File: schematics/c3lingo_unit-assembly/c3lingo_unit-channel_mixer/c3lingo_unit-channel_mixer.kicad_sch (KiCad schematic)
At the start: 94 parts, among them J301 Interconnect, J302 PowerSupply, J303 I/O, Q301 MMBFJ113, SW301 OnAir_X, SW302 Mute_X, U301 TL072, U302 LM339, U303 LM339, U304 LM339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

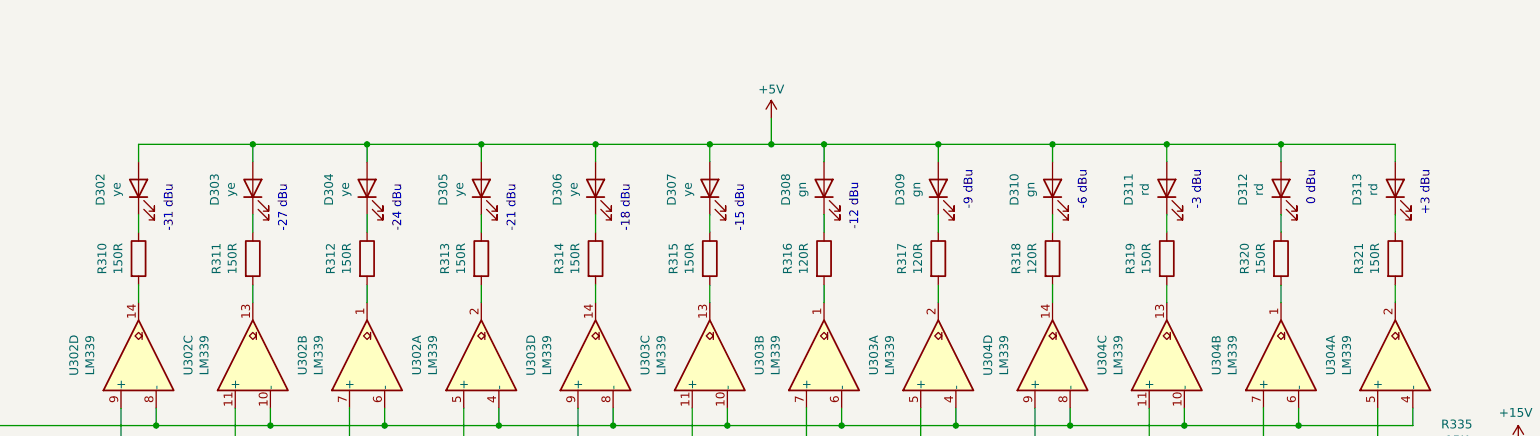
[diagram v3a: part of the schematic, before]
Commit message: Channel-Mixer: Change VU meter LEDs footprint to 5x2mm THD
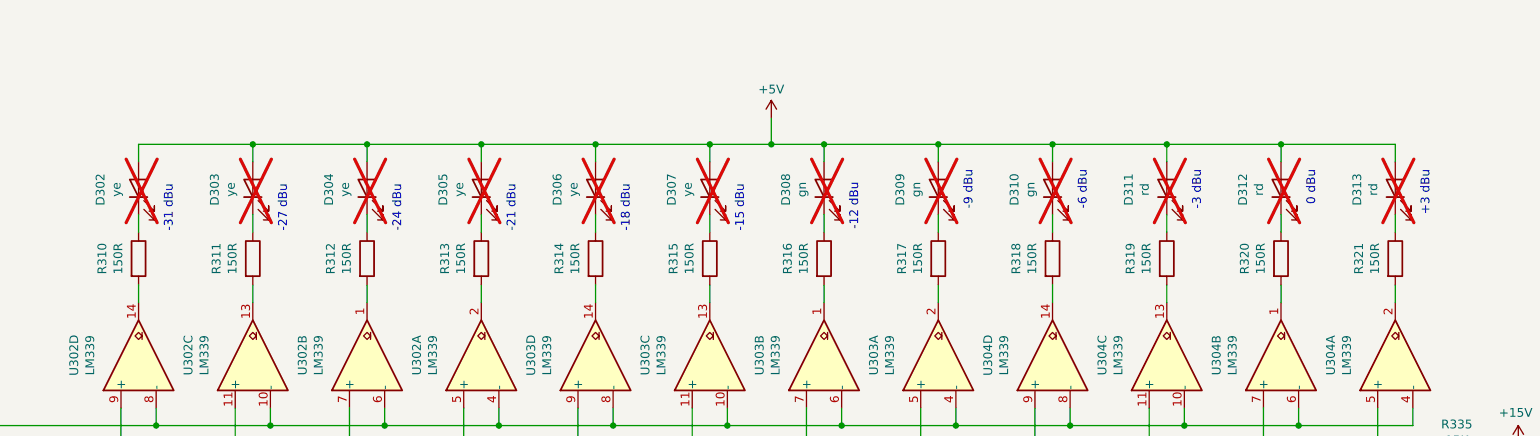
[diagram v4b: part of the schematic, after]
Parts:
- D302, D303, D304, D305, D306, D307: footprint LED_SMD:LED_0805_2012Metric_Pad1.15x1.40mm_HandSolder -> LED_THT:LED_Rectangular_W5.0mm_H2.0mm; LCSC Part # C2296 -> (none); Model generic 20 mA, 2.1 V -> LTL-433Y (2.1 V, 20 mA) or WP113YDT (2.0 V, 20 mA); now not fitted
- D308, D309, D310: footprint LED_SMD:LED_0805_2012Metric_Pad1.15x1.40mm_HandSolder -> LED_THT:LED_Rectangular_W5.0mm_H2.0mm; Model generic 20 mA, 2.8-2.9 V -> LTL433G or WP113GDT (2.2 V, 20 mA); now not fitted
- D311, D312, D313: footprint LED_SMD:LED_0805_2012Metric_Pad1.15x1.40mm_HandSolder -> LED_THT:LED_Rectangular_W5.0mm_H2.0mm; LCSC Part # C84256 -> (none); Model generic 20 mA, 2.0 V -> LTL433HR or WP113IDT (2.0 V, 20 mA); now not fitted
- R316, R317, R318: value 120R -> 150R
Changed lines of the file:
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@@
 	(title_block
 		(title "c3lingo interpeter unit -- channel mixer")
-		(date "2024-12-18")
+		(date "2025-08-25")
 		(rev "v0.4.0-dev")
 		(company "Jannik Beyerstedt (jtbx)")
@@
 		(in_bom yes)
 		(on_board yes)
-		(dnp no)
+		(dnp yes)
 		(property "Reference" "D313"
 			(at 332.3082 156.3878 0)
@@
 			)
 		)
-		(property "Footprint" "LED_SMD:LED_0805_2012Metric_Pad1.15x1.40mm_HandSolder"
+		(property "Footprint" "LED_THT:LED_Rectangular_W5.0mm_H2.0mm"
 			(at 337.82 156.21 0)
 			(effects
@@
 			)
 		)
-		(property "Model" "generic 20 mA, 2.0 V"
+		(property "Model" "LTL433HR or WP113IDT (2.0 V, 20 mA)"
 			(at 337.82 156.21 0)
 			(effects
@@
 			)
 		)
-		(property "LCSC Part #" "C84256"
+		(property "LCSC Part #" ""
 			(at 337.82 156.21 0)
 			(effects
@@
 		(in_bom yes)
 		(on_board yes)
-		(dnp no)
+		(dnp yes)
 		(property "Reference" "D312"
 			(at 315.7982 156.3878 0)
@@
 			)
 		)
-		(property "Footprint" "LED_SMD:LED_0805_2012Metric_Pad1.15x1.40mm_HandSolder"
+		(property "Footprint" "LED_THT:LED_Rectangular_W5.0mm_H2.0mm"
 			(at 321.31 156.21 0)
 			(effects
@@
 			)
 		)
-		(property "Model" "generic 20 mA, 2.0 V"
+		(property "Model" "LTL433HR or WP113IDT (2.0 V, 20 mA)"
 			(at 321.31 156.21 0)
 			(effects
@@
 			)
 		)
-		(property "LCSC Part #" "C84256"
+		(property "LCSC Part #" ""
 			(at 321.31 156.21 0)
 			(effects
@@
 		(in_bom yes)
 		(on_board yes)
-		(dnp no)
+		(dnp yes)
 		(property "Reference" "D311"
 			(at 299.2882 156.3878 0)
@@
 			)
 		)
-		(property "Footprint" "LED_SMD:LED_0805_2012Metric_Pad1.15x1.40mm_HandSolder"
+		(property "Footprint" "LED_THT:LED_Rectangular_W5.0mm_H2.0mm"
 			(at 304.8 156.21 0)
 			(effects
@@
 			)
 		)
-		(property "Model" "generic 20 mA, 2.0 V"
+		(property "Model" "LTL433HR or WP113IDT (2.0 V, 20 mA)"
 			(at 304.8 156.21 0)
 			(effects
@@
 			)
 		)
-		(property "LCSC Part #" "C84256"
+		(property "LCSC Part #" ""
 			(at 304.8 156.21 0)
 			(effects
@@
 			)
 		)
-		(property "Value" "120R"
+		(property "Value" "150R"
 			(at 285.3436 166.37 90)
 			(effects
@@
 		(in_bom yes)
 		(on_board yes)
-		(dnp no)
+		(dnp yes)
 		(property "Reference" "D310"
 			(at 282.7782 156.3878 0)
@@
 			)
 		)
-		(property "Footprint" "LED_SMD:LED_0805_2012Metric_Pad1.15x1.40mm_HandSolder"
+		(property "Footprint" "LED_THT:LED_Rectangular_W5.0mm_H2.0mm"
 			(at 288.29 156.21 0)
 			(effects
@@
 			)
 		)
-		(property "Description" "needs 110R @5V"
+		(property "Description" "needs 150R @5V"
 			(at 288.29 156.21 0)
 			(effects
@@
 			)
 		)
-		(property "Model" "generic 20 mA, 2.8-2.9 V"
+		(property "Model" "LTL433G or WP113GDT (2.2 V, 20 mA)"
 			(at 288.29 156.21 0)
 			(effects
@@
 			)
 		)
-		(property "Value" "120R"
+		(property "Value" "150R"
 			(at 268.8336 166.37 90)
 			(effects
@@
 		(in_bom yes)
 		(on_board yes)
-		(dnp no)
+		(dnp yes)
 		(property "Reference" "D309"
 			(at 266.2682 156.3878 0)
@@
 			)
 		)
-		(property "Footprint" "LED_SMD:LED_0805_2012Metric_Pad1.15x1.40mm_HandSolder"
+		(property "Footprint" "LED_THT:LED_Rectangular_W5.0mm_H2.0mm"
 			(at 271.78 156.21 0)
 			(effects
@@
 			)
 		)
-		(property "Description" "needs 110R @5V"
+		(property "Description" "needs 150R @5V"
 			(at 271.78 156.21 0)
 			(effects
@@
 			)
 		)
-		(property "Model" "generic 20 mA, 2.8-2.9 V"
+		(property "Model" "LTL433G or WP113GDT (2.2 V, 20 mA)"
 			(at 271.78 156.21 0)
 			(effects
@@
 			)
 		)
-		(property "Value" "120R"
+		(property "Value" "150R"
 			(at 252.3236 166.37 90)
 			(effects
@@
 		(in_bom yes)
 		(on_board yes)
-		(dnp no)
+		(dnp yes)
 		(property "Reference" "D308"
 			(at 249.7582 156.3878 0)
@@
 			)
 		)
-		(property "Footprint" "LED_SMD:LED_0805_2012Metric_Pad1.15x1.40mm_HandSolder"
+		(property "Footprint" "LED_THT:LED_Rectangular_W5.0mm_H2.0mm"
 			(at 255.27 156.21 0)
 			(effects
@@
 			)
 		)
-		(property "Description" "needs 110R @5V"
+		(property "Description" "needs 150R @5V"
 			(at 255.27 156.21 0)
 			(effects
@@
 			)
 		)
-		(property "Model" "generic 20 mA, 2.8-2.9 V"
+		(property "Model" "LTL433G or WP113GDT (2.2 V, 20 mA)"
 			(at 255.27 156.21 0)
 			(effects
@@
 		(in_bom yes)
 		(on_board yes)
-		(dnp no)
+		(dnp yes)
 		(property "Reference" "D307"
 			(at 233.2482 156.3878 0)
@@
 			)
 		)
-		(property "Footprint" "LED_SMD:LED_0805_2012Metric_Pad1.15x1.40mm_HandSolder"
+		(property "Footprint" "LED_THT:LED_Rectangular_W5.0mm_H2.0mm"
 			(at 238.76 156.21 0)
 			(effects
@@
 			)
 		)
-		(property "Description" "needs 145R @5V"
+		(property "Description" "needs 150R @5V"
 			(at 238.76 156.21 0)
 			(effects
@@
 			)
 		)
-		(property "Model" "generic 20 mA, 2.1 V"
+		(property "Model" "LTL-433Y (2.1 V, 20 mA) or WP113YDT (2.0 V, 20 mA)"
 			(at 238.76 156.21 0)
 			(effects
@@
 			)
 		)
-		(property "LCSC Part #" "C2296"
+		(property "LCSC Part #" ""
 			(at 238.76 156.21 0)
 			(effects
@@
 		(in_bom yes)
 		(on_board yes)
-		(dnp no)
+		(dnp yes)
 		(property "Reference" "D306"
 			(at 216.7382 156.3878 0)
@@
 			)
 		)
-		(property "Footprint" "LED_SMD:LED_0805_2012Metric_Pad1.15x1.40mm_HandSolder"
+		(property "Footprint" "LED_THT:LED_Rectangular_W5.0mm_H2.0mm"
 			(at 222.25 156.21 0)
 			(effects
@@
 			)
 		)
-		(property "Description" "needs 145R @5V"
+		(property "Description" "needs 150R @5V"
 			(at 222.25 156.21 0)
 			(effects
@@
 			)
 		)
-		(property "Model" "generic 20 mA, 2.1 V"
+		(property "Model" "LTL-433Y (2.1 V, 20 mA) or WP113YDT (2.0 V, 20 mA)"
 			(at 222.25 156.21 0)
 			(effects
@@
 			)
 		)
-		(property "LCSC Part #" "C2296"
+		(property "LCSC Part #" ""
 			(at 222.25 156.21 0)
 			(effects
@@
 		(in_bom yes)
 		(on_board yes)
-		(dnp no)
+		(dnp yes)
 		(property "Reference" "D305"
 			(at 200.2282 156.3878 0)
@@
 			)
 		)
-		(property "Footprint" "LED_SMD:LED_0805_2012Metric_Pad1.15x1.40mm_HandSolder"
+		(property "Footprint" "LED_THT:LED_Rectangular_W5.0mm_H2.0mm"
 			(at 205.74 156.21 0)
 			(effects
@@
 			)
 		)
-		(property "Description" "needs 145R @5V"
+		(property "Description" "needs 150R @5V"
 			(at 205.74 156.21 0)
 			(effects
@@
 			)
 		)
-		(property "Model" "generic 20 mA, 2.1 V"
+		(property "Model" "LTL-433Y (2.1 V, 20 mA) or WP113YDT (2.0 V, 20 mA)"
 			(at 205.74 156.21 0)
 			(effects
@@
 			)
 		)
-		(property "LCSC Part #" "C2296"
+		(property "LCSC Part #" ""
 			(at 205.74 156.21 0)
 			(effects
@@
 		(in_bom yes)
 		(on_board yes)
-		(dnp no)
+		(dnp yes)
 		(property "Reference" "D304"
 			(at 183.7182 156.3878 0)
@@
 			)
 		)
-		(property "Footprint" "LED_SMD:LED_0805_2012Metric_Pad1.15x1.40mm_HandSolder"
+		(property "Footprint" "LED_THT:LED_Rectangular_W5.0mm_H2.0mm"
 			(at 189.23 156.21 0)
 			(effects
@@
 			)
 		)
-		(property "Description" "needs 145R @5V"
+		(property "Description" "needs 150R @5V"
 			(at 189.23 156.21 0)
 			(effects
@@
 			)
 		)
-		(property "Model" "generic 20 mA, 2.1 V"
+		(property "Model" "LTL-433Y (2.1 V, 20 mA) or WP113YDT (2.0 V, 20 mA)"
 			(at 189.23 156.21 0)
 			(effects
@@
 			)
 		)
-		(property "LCSC Part #" "C2296"
+		(property "LCSC Part #" ""
 			(at 189.23 156.21 0)
 			(effects
@@
 		(in_bom yes)
 		(on_board yes)
-		(dnp no)
+		(dnp yes)
 		(property "Reference" "D303"
 			(at 167.2082 156.3878 0)
@@
 			)
 		)
-		(property "Footprint" "LED_SMD:LED_0805_2012Metric_Pad1.15x1.40mm_HandSolder"
+		(property "Footprint" "LED_THT:LED_Rectangular_W5.0mm_H2.0mm"
 			(at 172.72 156.21 0)
 			(effects
@@
 			)
 		)
-		(property "Description" "needs 145R @5V"
+		(property "Description" "needs 150R @5V"
 			(at 172.72 156.21 0)
 			(effects
@@
 			)
 		)
-		(property "Model" "generic 20 mA, 2.1 V"
+		(property "Model" "LTL-433Y (2.1 V, 20 mA) or WP113YDT (2.0 V, 20 mA)"
 			(at 172.72 156.21 0)
 			(effects
@@
 			)
 		)
-		(property "LCSC Part #" "C2296"
+		(property "LCSC Part #" ""
 			(at 172.72 156.21 0)
 			(effects
@@
 		(in_bom yes)
 		(on_board yes)
-		(dnp no)
+		(dnp yes)
 		(property "Reference" "D302"
 			(at 150.6982 156.3878 0)
@@
 			)
 		)
-		(property "Footprint" "LED_SMD:LED_0805_2012Metric_Pad1.15x1.40mm_HandSolder"
+		(property "Footprint" "LED_THT:LED_Rectangular_W5.0mm_H2.0mm"
 			(at 156.21 156.21 0)
 			(effects
@@
 			)
 		)
-		(property "Description" "needs 145R @5V"
+		(property "Description" "needs 150R @5V"
 			(at 156.21 156.21 0)
 			(effects
@@
 			)
 		)
-		(property "Model" "generic 20 mA, 2.1 V"
+		(property "Model" "LTL-433Y (2.1 V, 20 mA) or WP113YDT (2.0 V, 20 mA)"
 			(at 156.21 156.21 0)
 			(effects
@@
 			)
 		)
-		(property "LCSC Part #" "C2296"
+		(property "LCSC Part #" ""
 			(at 156.21 156.21 0)
 			(effects

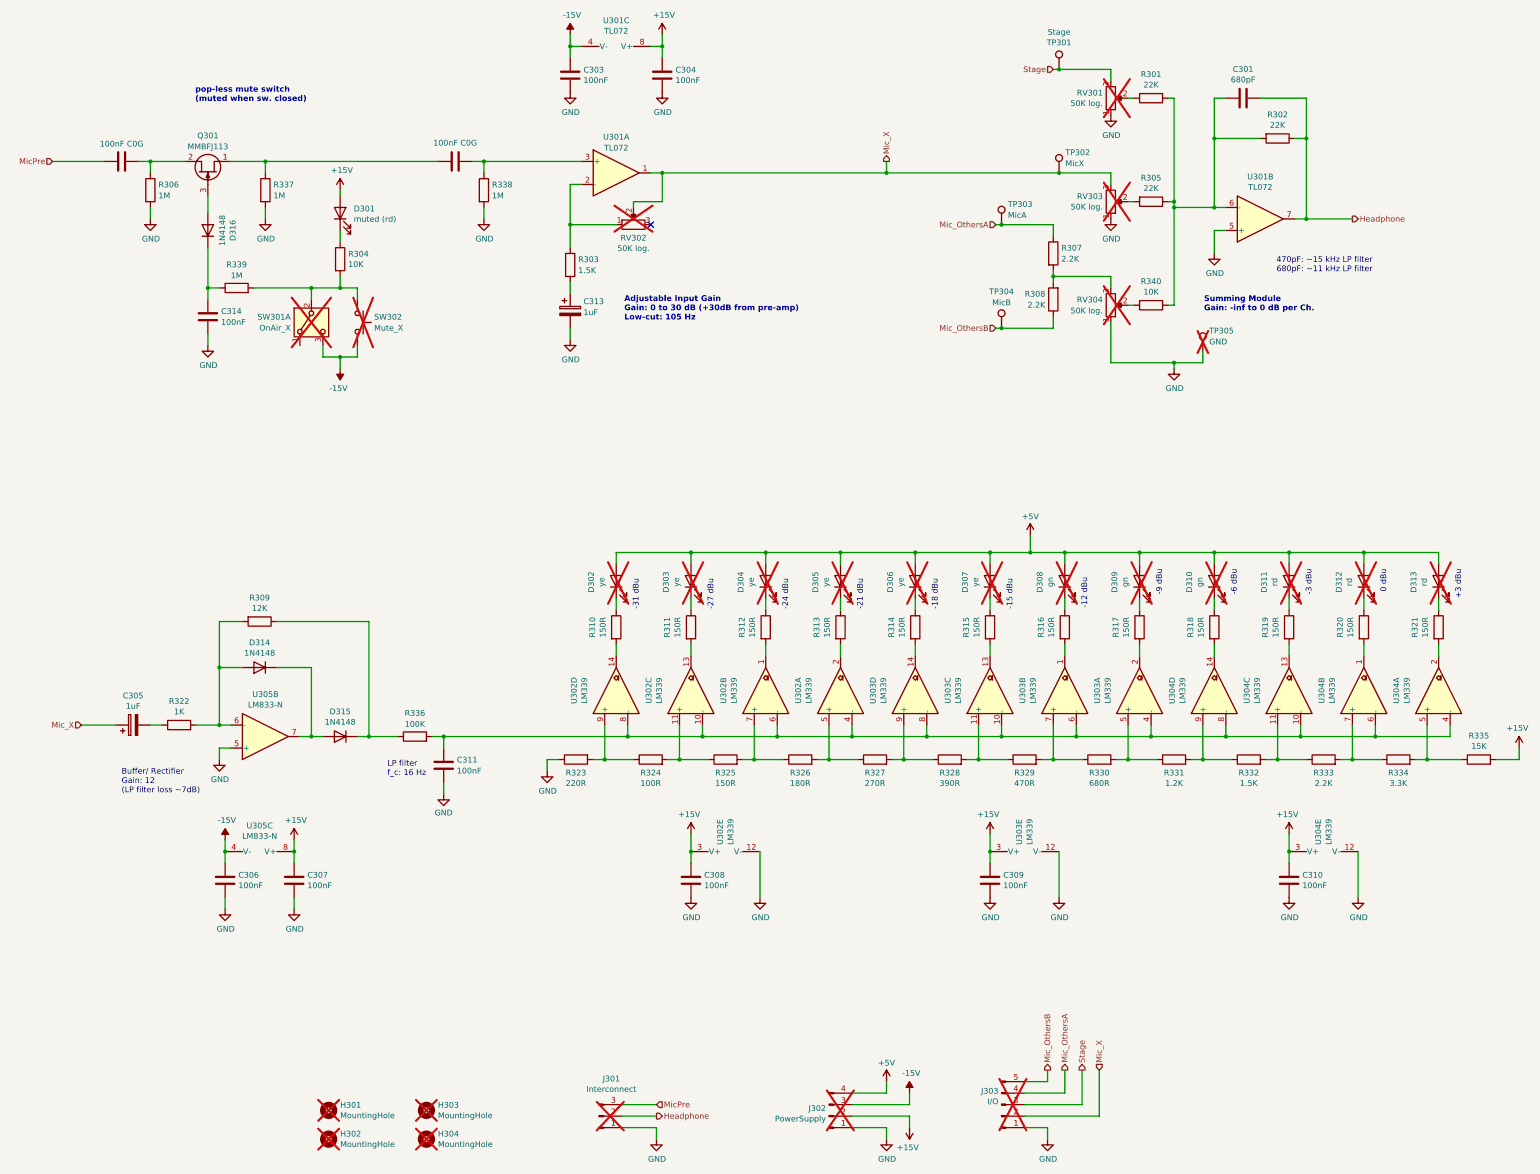
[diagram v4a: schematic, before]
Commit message: Change inter-PCB connections to IDC connectors
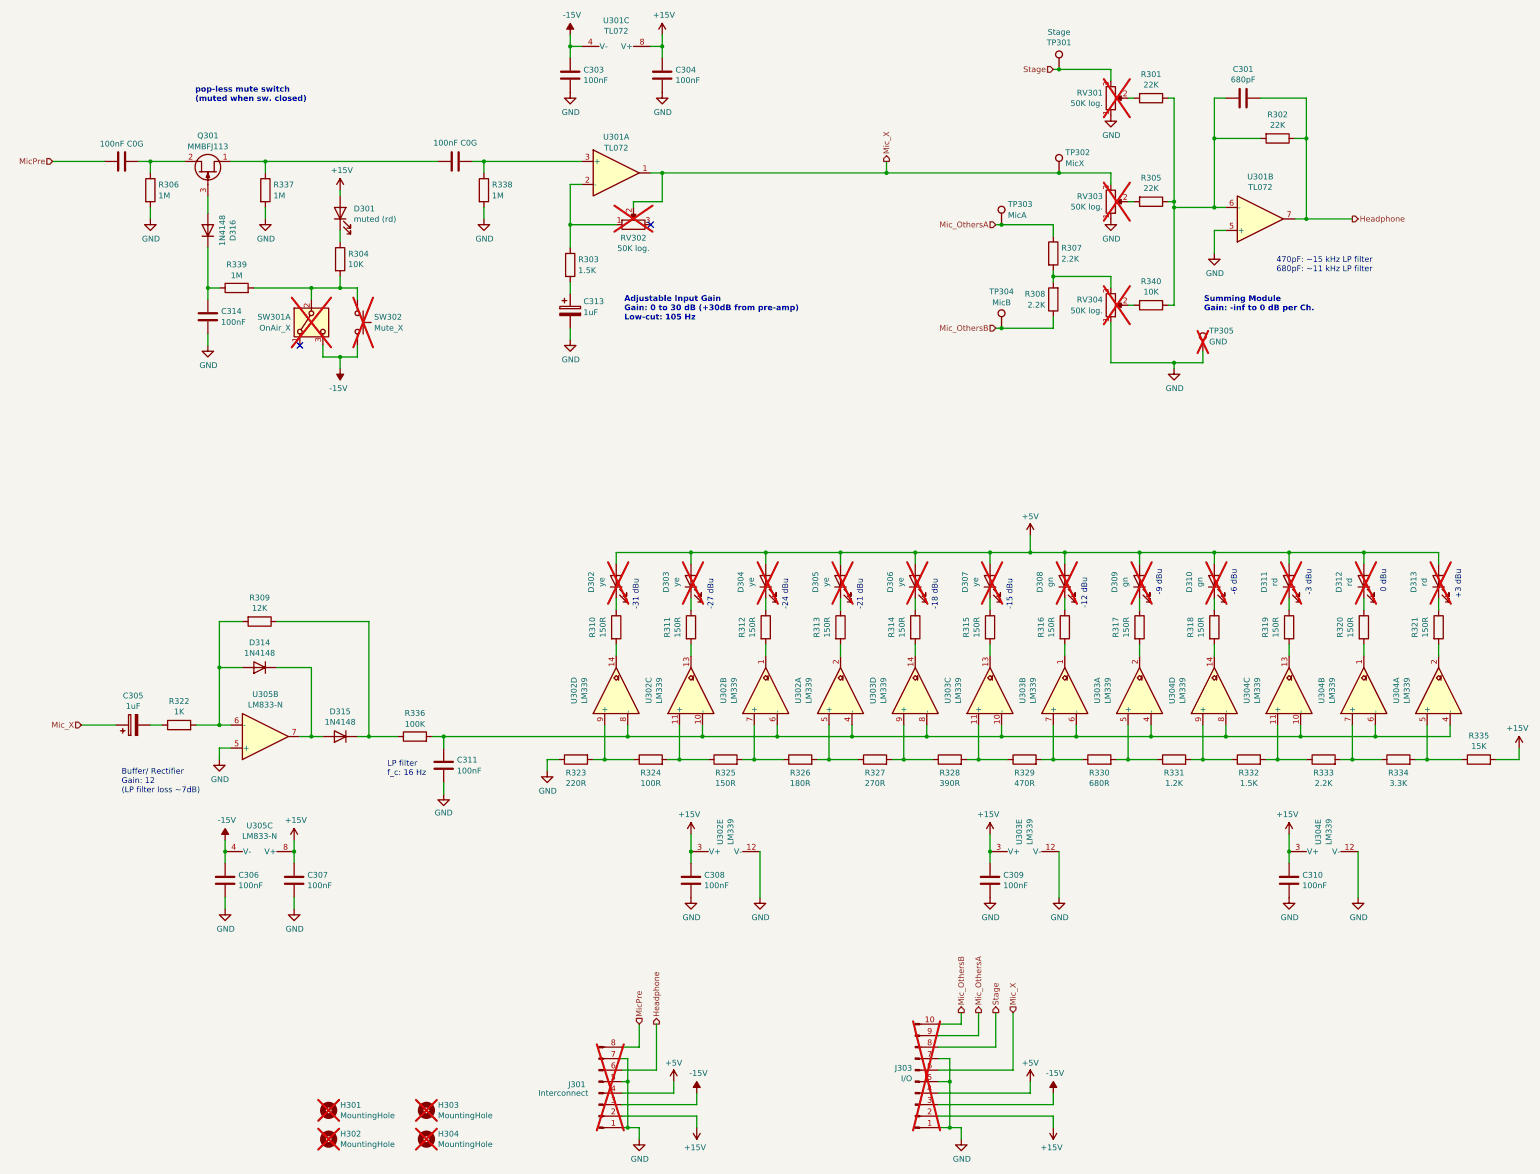
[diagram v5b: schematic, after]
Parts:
- removed J302: PowerSupply, TerminalBlock_Phoenix:TerminalBlock_Phoenix_PTSM-0,5-4-2.5-H-THR_1x04_P2.50mm_Horizontal, symbol Connector:Conn_01x04_Pin
- J301: footprint TerminalBlock_Phoenix:TerminalBlock_Phoenix_PTSM-0,5-3-2.5-H-THR_1x03_P2.50mm_Horizontal -> Connector_IDC:IDC-Header_2x04_P2.54mm_Horizontal; symbol Connector:Conn_01x03_Pin -> Connector:Conn_01x08_Pin; Model PTSM 0,5/ 3-2,5-H THR -> Generic IDC Connector
- J303: footprint TerminalBlock_Phoenix:TerminalBlock_Phoenix_PTSM-0,5-5-2.5-H-THR_1x05_P2.50mm_Horizontal -> Connector_IDC:IDC-Header_2x05_P2.54mm_Horizontal; symbol Connector:Conn_01x05_Pin -> Connector:Conn_01x10_Pin; Model PTSM 0,5/ 5-2,5-H THR -> Generic IDC Connector
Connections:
- net +15V: now also J301.2 (Pin_2), J303.2 (Pin_2)
- net +5V: now also J301.4 (Pin_4), J303.4 (Pin_4)
- net -15V: now also J301.3 (Pin_3), J303.3 (Pin_3)
- net GND: now also J301.5 (Pin_5), J301.7 (Pin_7), J303.5 (Pin_5), J303.7 (Pin_7)
- net Headphone: now also J301.6 (Pin_6); no longer J301.2 (Pin_2)
- net MicPre: now also J301.8 (Pin_8); no longer J301.3 (Pin_3)
- net Mic_OthersA: now also J303.9 (Pin_9); no longer J303.4 (Pin_4)
- net Mic_OthersB: now also J303.10 (Pin_10); no longer J303.5 (Pin_5)
- net Mic_X: now also J303.6 (Pin_6); no longer J303.2 (Pin_2)
- net Stage: now also J303.8 (Pin_8); no longer J303.3 (Pin_3)
- no-connect marks 1 -> 2
